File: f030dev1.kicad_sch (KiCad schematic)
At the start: 5 parts, among them J1 Conn_01x10_Pin, J2 Conn_01x03_Pin, U1 STM32F030F4Px, U2 74HC595, U3 AMS1117-3.3

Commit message: в процесе
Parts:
- added J3: Conn_01x08_Pin, main:PinHeader_2x04_P2.54mm_Vertical, symbol Connector:Conn_01x08_Pin
- J1: footprint main:PinHeader_2x05_P2.00mm_Vertical -> main:PinHeader_2x05_P2.54mm_Vertical
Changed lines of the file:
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@@
 			)
 		)
-		(property "Footprint" "main:PinHeader_2x05_P2.00mm_Vertical"
+		(property "Footprint" "main:PinHeader_2x05_P2.54mm_Vertical"
 			(at 88.9 66.04 0)
 			(effects
@@
 					(unit 1)
 				)
+			)
+		)
+	)
+	(symbol
+		(lib_id "Connector:Conn_01x08_Pin")
+		(at 222.25 68.58 0)
+		(unit 1)
+		(exclude_from_sim no)
+		(in_bom yes)
+		(on_board yes)
+		(dnp no)
+		(fields_autoplaced yes)
+		(property "Reference" "J3"
+			(at 222.885 55.88 0)
+			(effects
+				(font
+					(size 1.27 1.27)
+				)
+			)
+		)
+		(property "Value" "Conn_01x08_Pin"
+			(at 222.885 58.42 0)
+			(effects
+				(font
+					(size 1.27 1.27)
+				)
+			)
+		)
+		(property "Footprint" "main:PinHeader_2x04_P2.54mm_Vertical"
+			(at 222.25 68.58 0)
+			(effects
+				(font
+					(size 1.27 1.27)
+				)
+				(hide yes)
+			)
+		)
+		(property "Datasheet" "~"
+			(at 222.25 68.58 0)
+			(effects
+				(font
+					(size 1.27 1.27)
+				)
+				(hide yes)
+			)
+		)
+		(property "Description" "Generic connector, single row, 01x08, script generated"
+			(at 222.25 68.58 0)
+			(effects
+				(font
+					(size 1.27 1.27)
+				)
+				(hide yes)
+			)
+		)
+		(pin "1"
+		)
+		(pin "5"
+		)
+		(pin "4"
+		)
+		(pin "8"
+		)
+		(pin "6"
+		)
+		(pin "2"
+		)
+		(pin "7"
+		)
+		(pin "3"
+		)
+		(instances
+			(project ""
+				(path "/45100149-715c-43f3-a12c-de58f75aa811"
+					(reference "J3")
+					(unit 1)
+				)

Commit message: Старт
схему нужно проверять
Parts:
- removed J1: Conn_01x10_Pin, main:PinHeader_2x05_P2.54mm_Vertical, symbol Connector:Conn_01x10_Pin
- removed J3: Conn_01x08_Pin, main:PinHeader_2x04_P2.54mm_Vertical, symbol Connector:Conn_01x08_Pin
- added C1, C4: C_Polarized, Capacitor_THT:CP_Radial_D7.5mm_P2.50mm, symbol Device:C_Polarized
- added C2, C3: C_Small, Capacitor_SMD:C_0805_2012Metric_Pad1.18x1.45mm_HandSolder, symbol Device:C_Small
- added J2: Conn_01x02_Pin, main:PinHeader_1x02_P2.54mm_Vertical, symbol Connector:Conn_01x02_Pin
- added J3: Conn_01x06_Pin, main:PinHeader_1x06_P2.54mm_Vertical, symbol Connector:Conn_01x06_Pin
- added J4: Conn_01x10_Pin, main:PinHeader_2x05_P2.54mm_Vertical, symbol Connector:Conn_01x10_Pin
- renumbered J2 to J1, U3 to U2, U2 to U3
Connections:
- net at U3.1 (QB): now also J4.2 (Pin_2)
- net +3.3V: now reaches U3.10 (~{SRCLR})
- net +3.3V: now also J1.1 (Pin_1), U1.16 (VDD), U1.5 (VDDA), U2.2 (VO), U3.16 (VCC), C2.2, C3.2, C4.1, J3.1 (Pin_1)
- net CLK_595: now reaches U3.11 (SRCLK)
- net CLK_595: now also U1.12 (PA6)
- net CS_595: now reaches U3.12 (RCLK)
- net CS_595: now also U1.11 (PA5)
- net GNDREF: now reaches U3.13 (~{OE})
- net GNDREF: now also J1.3 (Pin_3), U1.1 (BOOT0), U1.15 (VSS), U2.1 (GND), U3.8 (GND), C1.2, C2.1, C3.1, C4.2, J2.2 (Pin_2), J3.6 (Pin_6), J4.10 (Pin_10), J4.9 (Pin_9)
- net DAT_595: now reaches U3.14 (SER)
- net DAT_595: now also U1.13 (PA7)
- net at U3.15 (QA): now also J4.1 (Pin_1)
- net at U3.2 (QC): now also J4.3 (Pin_3)
- net at U3.3 (QD): now also J4.4 (Pin_4)
- net at U3.4 (QE): now also J4.5 (Pin_5)
- net at U3.5 (QF): now also J4.6 (Pin_6)
- net at U3.6 (QG): now also J4.7 (Pin_7)
- net at U3.7 (QH): now also J4.8 (Pin_8)
- net RX: now reaches J1.2 (Pin_2)
- net RX: now also U1.6 (PA0)
- net button_4: now reaches U1.10 (PA4)
- net button_4: now also J3.5 (Pin_5)
- net button_1: now reaches U1.7 (PA1)
- net button_1: now also J3.2 (Pin_2)
- net button_2: now reaches U1.8 (PA2)
- net button_2: now also J3.3 (Pin_3)
- net button_3: now reaches U1.9 (PA3)
- net button_3: now also J3.4 (Pin_4)
- net +5V: now reaches U2.3 (VI)
- net +5V: now also C1.1, J2.1 (Pin_1)
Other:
- moved on the sheet: J1, U3

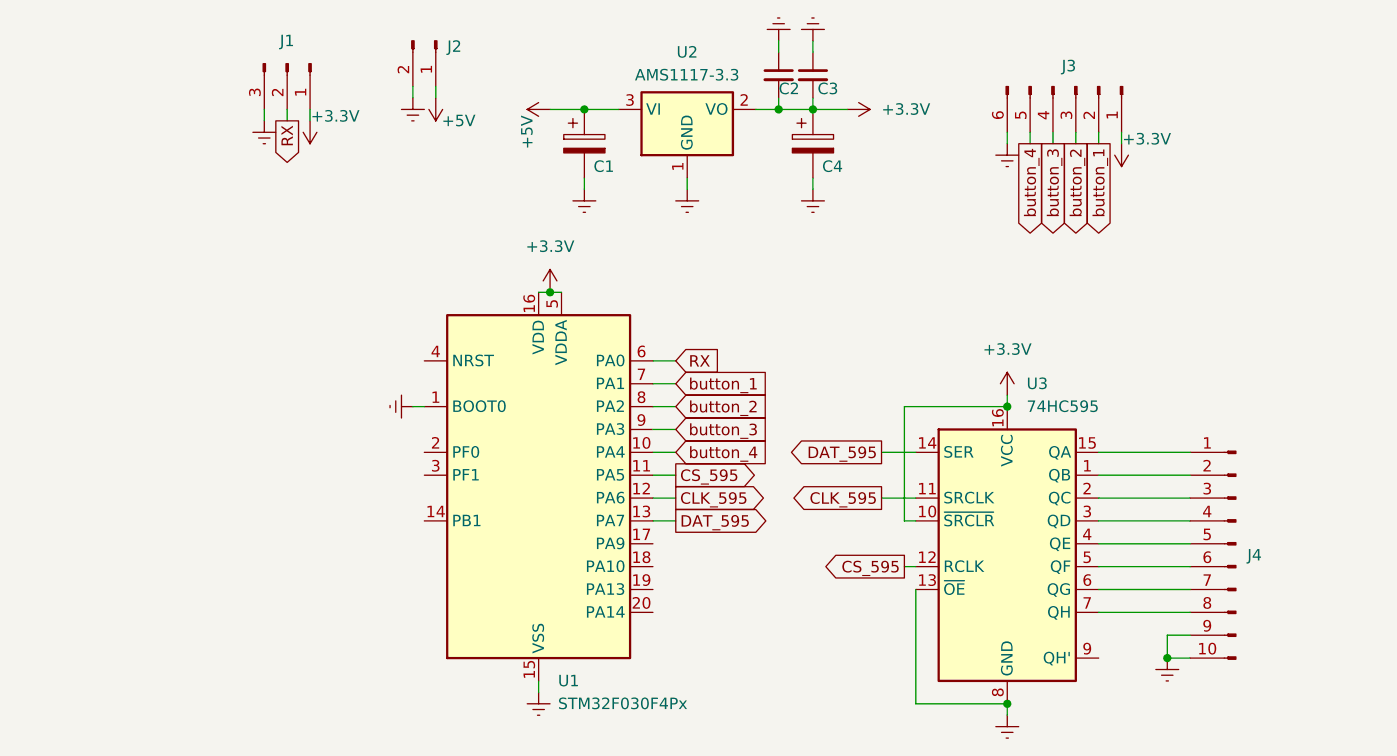
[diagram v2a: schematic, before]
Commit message: SWDIO add
добавлен разъем для программирования
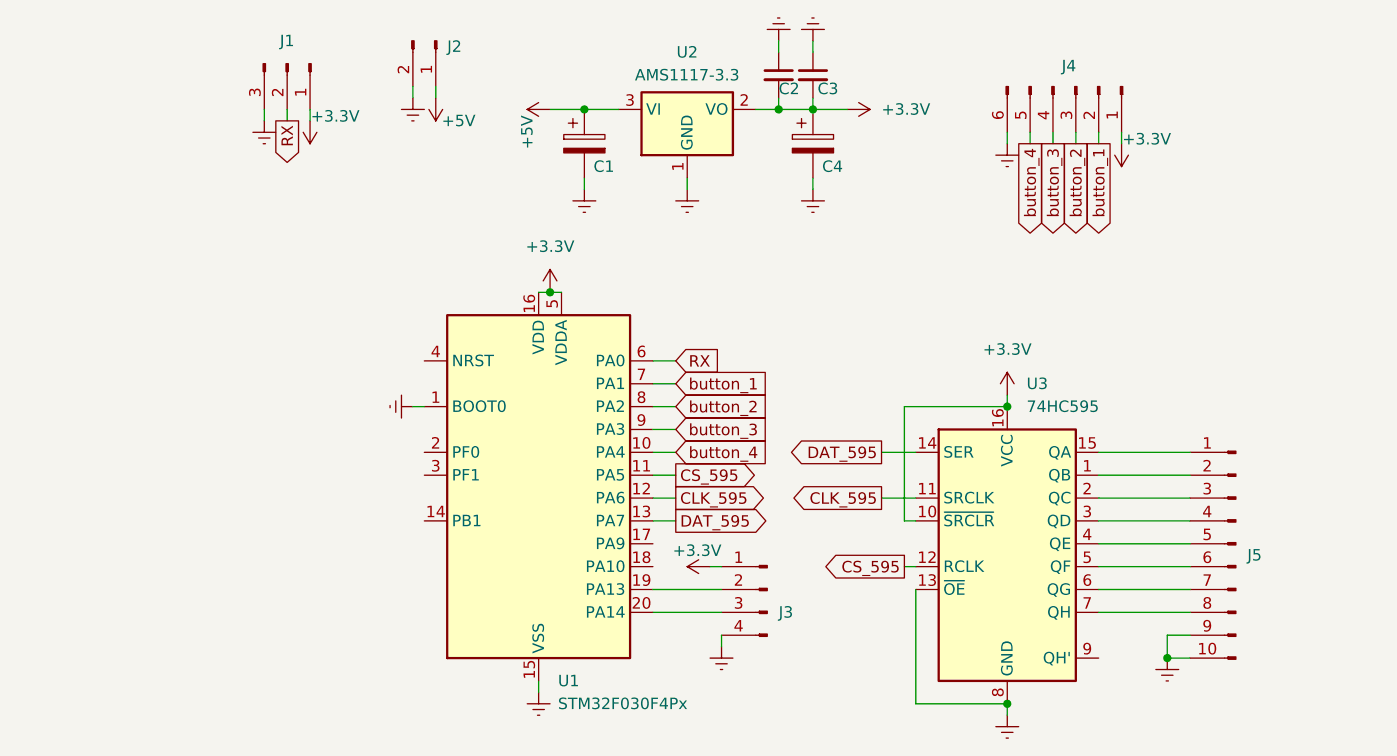
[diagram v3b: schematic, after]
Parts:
- added J3: Conn_01x04_Pin, main:PinHeader_1x04_P2.54mm_Vertical, symbol Connector:Conn_01x04_Pin
- renumbered J3 to J4, J4 to J5
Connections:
- net +3.3V: now also J3.1 (Pin_1)
- net GNDREF: now also J3.4 (Pin_4)
- net at U1.19 (PA13): now also J3.2 (Pin_2)
- net at U1.20 (PA14): now also J3.3 (Pin_3)
